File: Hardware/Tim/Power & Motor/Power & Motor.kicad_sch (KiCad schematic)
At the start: 86 parts, among them Q1 BSC520N15NS3, Q2 BSC520N15NS3, Q3 BSC093N15NS5, Q4 BSC093N15NS5, Q5 BSC520N15NS3, Q6 BSC520N15NS3, Q7 BSC093N15NS5, Q8 BSC093N15NS5, U1 LTC7810, U2 LTC7810, U3 LTC6908-2

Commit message: motor controller and h-bridge stuff
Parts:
- added C53, C54, C59: 0.1uF, symbol Device:C_Small
- added C55, C56: 1uF, symbol Device:C_Small
- added C57: 47uF, symbol Device:C_Polarized_Small
- added C58: 150uF, symbol Device:C_Polarized_Small
- added M1: Motor_DC_ALT, symbol Motor:Motor_DC_ALT
- added Q10, Q11, Q12, Q9: Q_NMOS_SGD, symbol Device:Q_NMOS_SGD
- added R10: 10K, symbol Device:R_Small
- added R7: idk, symbol Device:R_Small
- added U4: DRV8714, DRV8714_RHA_TEX, symbol BPP_Lib:DRV8714
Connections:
- net GND: now also C56.2, C57.2, C58.2, C59.2, Q10.1 (S), Q12.1 (S), U4.19 (PGND1), U4.37 (GND), U4.41 (GND)
- net +24V: no longer names the net of C37.2, C38.1, C40.1, C41.1, C42.1, C43.1, C44.1, C45.1, C46.1, C47.1, C48.1, L3.2, L4.2, R14.1, R15.2, R16.1, U2.1 (SENSE1-), U2.11 (EXTVCC), U2.12 (SENSE2-)
- net +24V: no longer C16.1, C17.1, C18.1, C19.1, C2.2, C20.1, C21.1, C22.1, C23.1, C3.1, L1.2, L2.2, R3.1, R4.2, R5.1, U1.1 (SENSE1-), U1.11 (EXTVCC), U1.12 (SENSE2-)
- new net: C53.1, U4.26 (CP1H)
- new net: C53.2, U4.25 (CP1L)
- new net: C54.2, U4.23 (CP2L)
- new net: C54.1, U4.24 (CP2H)
- new net: C55.2, U4.27 (VCP)
- new net BRAKE: U4.11 (BRAKE)
- new net FAULT: R10.2, U4.8 (NFLT)
- new net GH1: Q9.2 (G), U4.16 (GH1)
- new net GH2: Q11.2 (G), U4.22 (GH2)
- new net GL1: Q10.2 (G), U4.18 (GL1)
- new net GL2: Q12.2 (G), U4.20 (GL2)
- new net IN1: U4.3 (IN1/EN1)
- new net IN2: U4.4 (IN2/PH1)
- new net NSLEEP: U4.7 (NSLEEP)
- new net SH1: Q10.3 (D), Q9.1 (S), R7.1, U4.12 (SP1), U4.17 (SH1)
- new net SH2: M1.2 (-), Q11.1 (S), Q12.3 (D), U4.21 (SH2)
- new net SN1: M1.1 (+), R7.2, U4.13 (SN1)
- new net SO1: U4.9 (SO1)
- new net VCC: C16.1, C17.1, C18.1, C19.1, C2.2, C20.1, C21.1, C22.1, C23.1, C3.1, C55.1, C56.1, C57.1, C58.1, C59.1, L1.2, L2.2, Q11.3 (D), Q9.3 (D), R10.1, R3.1, R4.2, R5.1, U1.1 (SENSE1-), U1.11 (EXTVCC), U1.12 (SENSE2-), U4.28 (PVDD), U4.38 (DVDD)
- no-connect marks 2 -> 15
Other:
- note added: "0.1uF x 2"
- note added: "20V Dual Phase, Single Output, Step-Down Regulator"
- note added: "H-Bridge"
- note added: "Motor Controller"
- note added: "Motor Driver"
- note added: "Switching Controller"
- note removed: "20V Four Phase, Single Output, Step-Down Regulator"
- note removed: "Switching Controllers"
- moved on the sheet: BT1, C24, C25, C26, C27, C28, C29, C30, C31, C32, C33, C34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

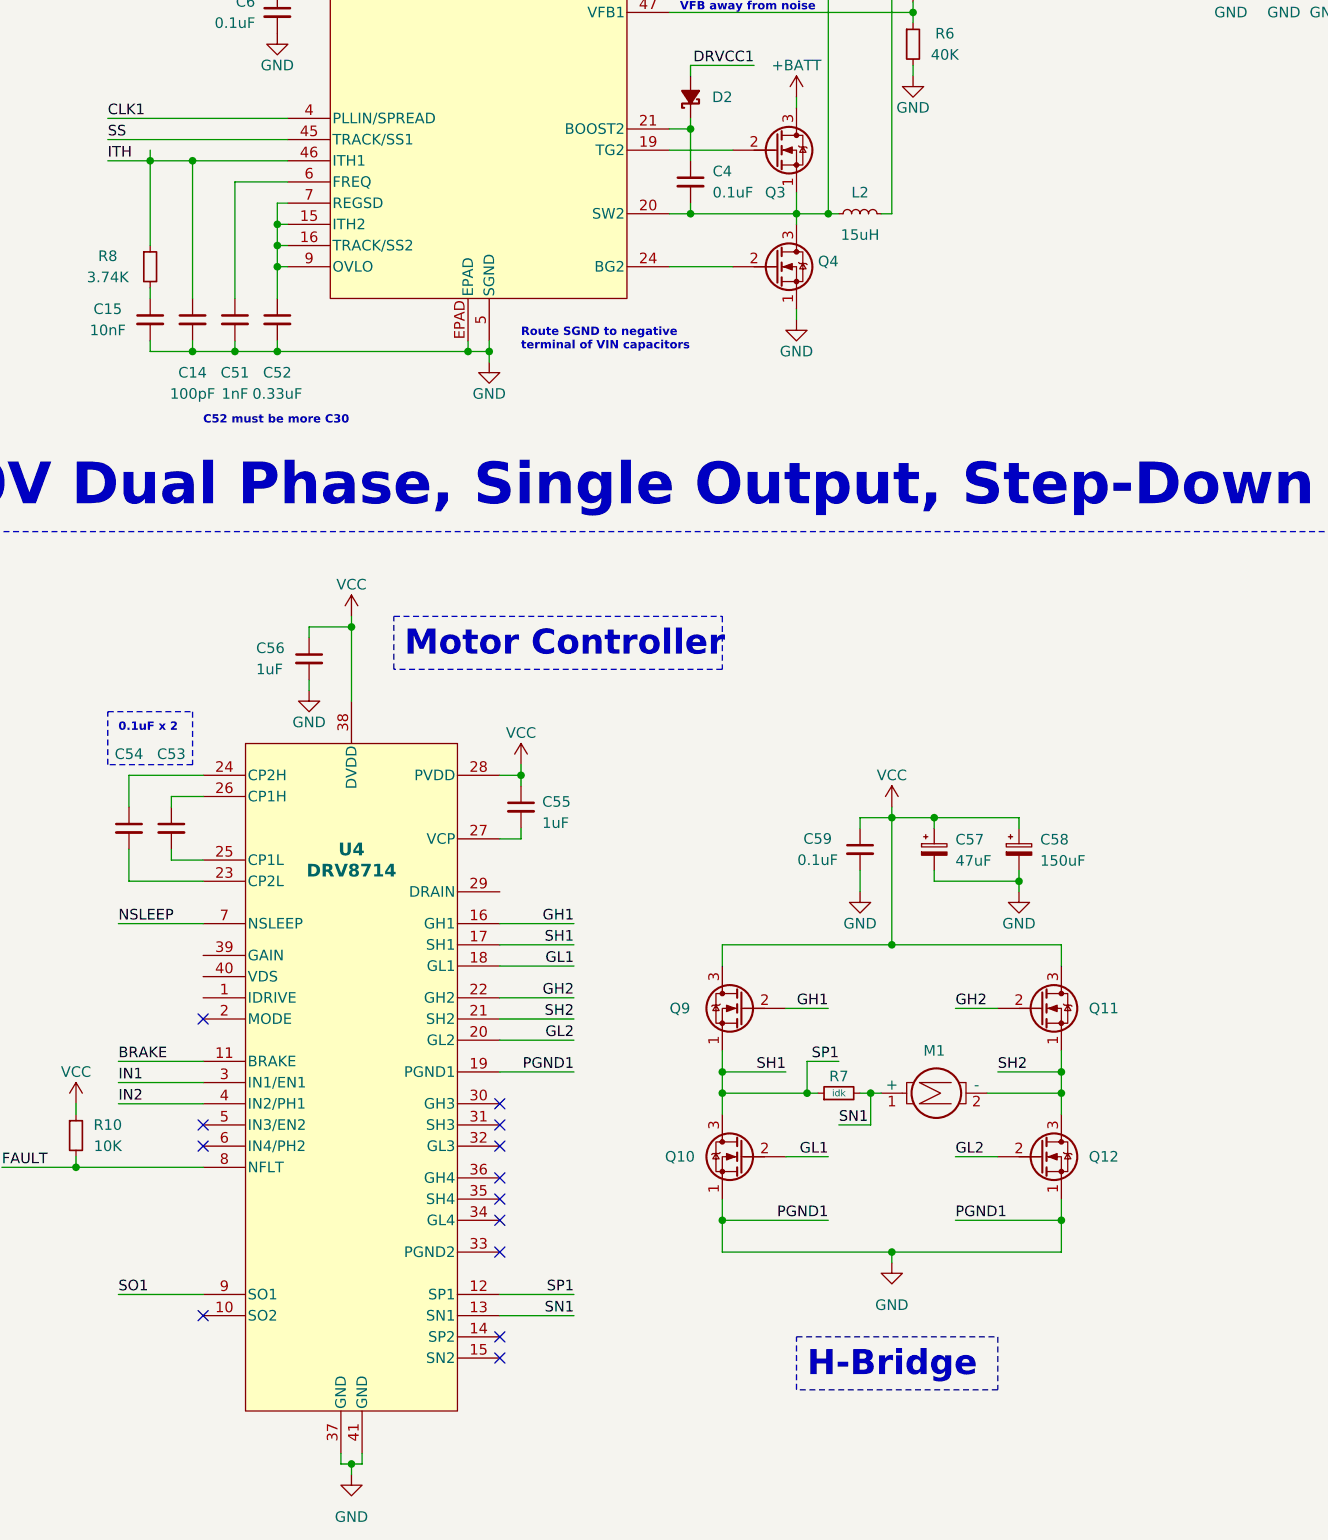
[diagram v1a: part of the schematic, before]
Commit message: more h-bridge shenanigans and 2 phase power (cringe)
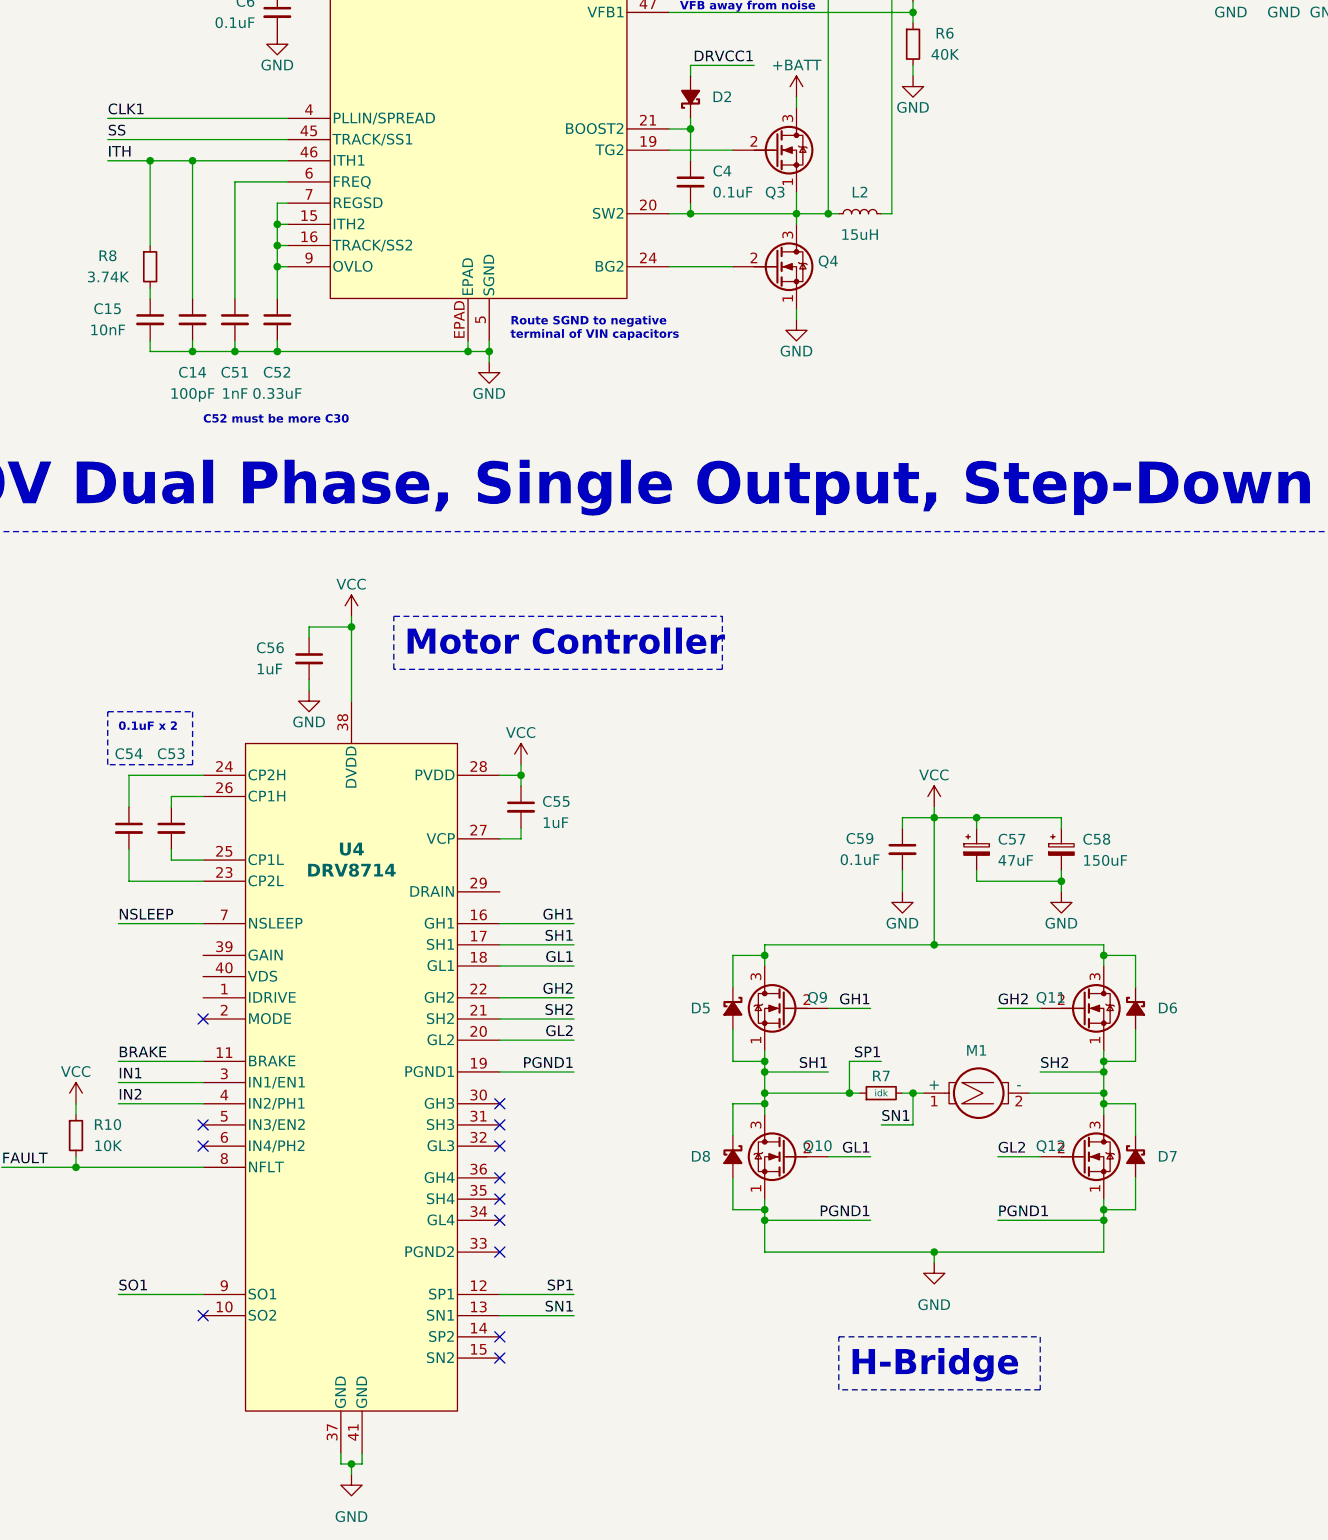
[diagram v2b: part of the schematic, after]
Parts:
- added D5, D6, D7, D8: D_Schottky_Small_Filled, symbol Device:D_Schottky_Small_Filled
- Q10, Q11, Q12, Q9: value Q_NMOS_SGD -> BSC010N04LSATMA1; footprint (none) -> BPP_Lib:Infineon 8-PowerTDFN
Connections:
- net GND: now also D7.2 (A), D8.2 (A)
- net SH1: now also D5.2 (A), D8.1 (K)
- net SH2: now also D6.2 (A), D7.1 (K)
- net VCC: now also D5.1 (K), D6.1 (K)
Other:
- moved on the sheet: C57, C58, C59, M1, Q10, Q11, Q12, Q9, R7

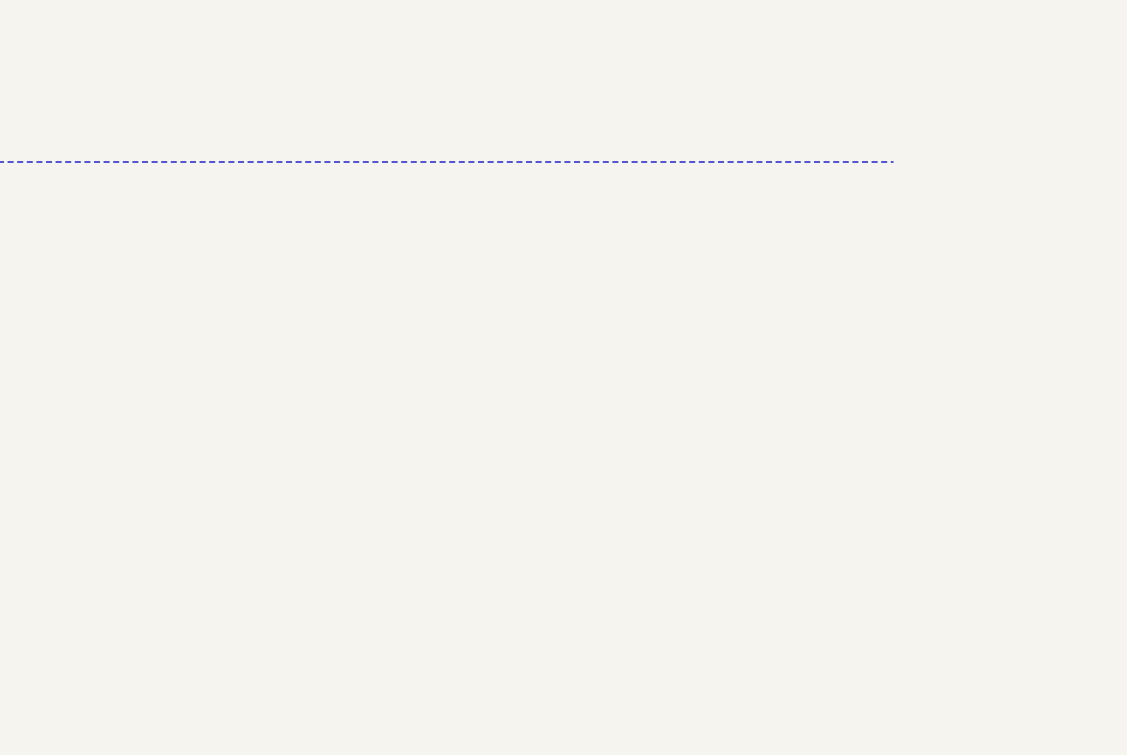
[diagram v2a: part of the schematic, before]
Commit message: Made it all one board due to large space allowed
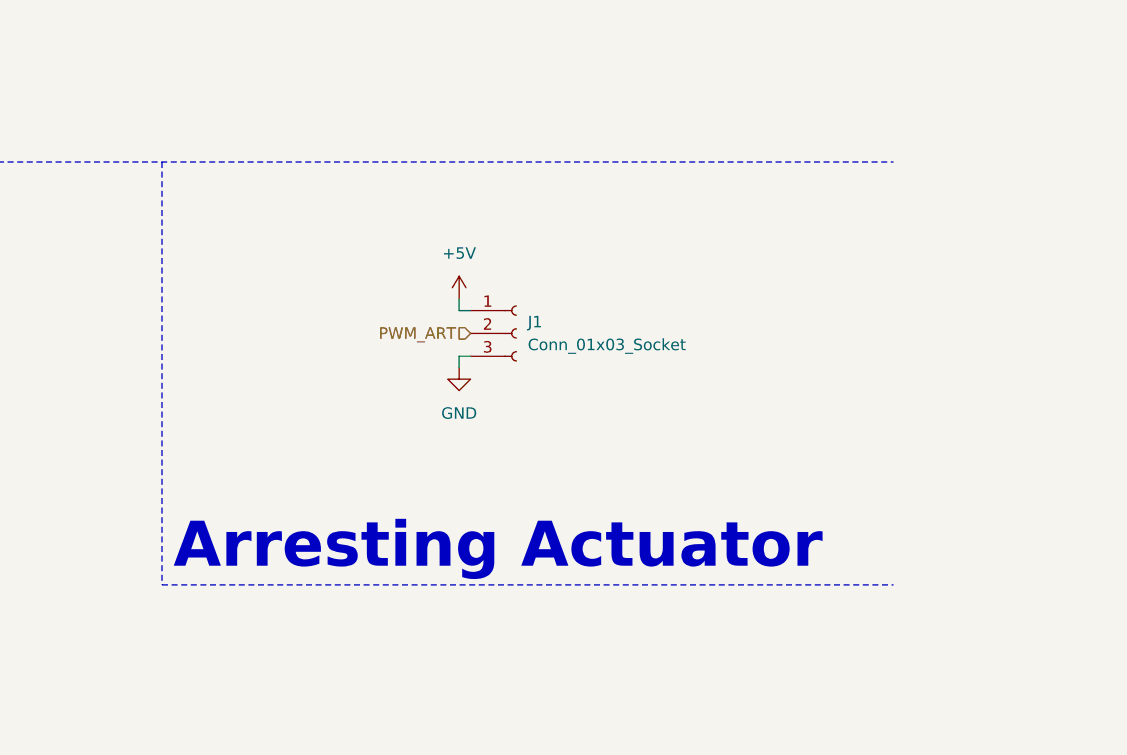
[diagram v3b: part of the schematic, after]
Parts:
- added J1: Conn_01x03_Socket, symbol Connector:Conn_01x03_Socket
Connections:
- net GND: now also J1.3 (Pin_3)
- new net +5V: J1.1 (Pin_1)
- new net PWM_ART: J1.2 (Pin_2)
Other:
- note added: "Arresting Actuator"
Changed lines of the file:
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@@
     (stroke (width 0) (type default))
   )
+  (wire (pts (xy 360.68 171.45) (xy 359.41 171.45))
+    (stroke (width 0) (type default))
+  )
   (wire (pts (xy 497.84 -19.05) (xy 492.76 -19.05))
     (stroke (width 0) (type default))
@@
     (stroke (width 0) (type default))
   )
+  (wire (pts (xy 359.41 166.37) (xy 360.68 166.37))
+    (stroke (width 0) (type default))
+  )
   (wire (pts (xy 110.49 69.85) (xy 110.49 71.12))
     (stroke (width 0) (type default))
@@
     (stroke (width 0) (type default))
   )
+  (wire (pts (xy 359.41 171.45) (xy 359.41 172.72))
+    (stroke (width 0) (type default))
+  )
   (wire (pts (xy 114.3 217.17) (xy 124.46 217.17))
     (stroke (width 0) (type default))
@@
     (stroke (width 0) (type default))
   )
+  (wire (pts (xy 359.41 165.1) (xy 359.41 166.37))
+    (stroke (width 0) (type default))
+  )
   (wire (pts (xy 55.88 78.74) (xy 55.88 83.82))
     (stroke (width 0) (type default))
@@
     (stroke (width 0) (type default))
   )
+  (polyline (pts (xy 326.39 149.86) (xy 326.39 196.85))
+    (stroke (width 0) (type dash_dot))
+  )
   (wire (pts (xy 55.88 76.2) (xy 55.88 78.74))
     (stroke (width 0) (type default))
@@
     (stroke (width 0) (type default))
   )
+  (polyline (pts (xy 326.39 196.85) (xy 407.67 196.85))
+    (stroke (width 0) (type dash_dot))
+  )
   (wire (pts (xy 375.92 36.83) (xy 381 36.83))
     (stroke (width 0) (type default))
@@
     (effects (font (size 3 3) (thickness 0.6) bold) (justify left bottom))
   )
+  (text "Arresting Actuator" (at 327.66 195.58 0)
+    (effects (font (size 5 5) (thickness 1) bold) (justify left bottom))
+  )
   (text "330uF x 2" (at 175.26 68.58 0)
     (effects (font (size 1 1) (thickness 0.2) bold) (justify left bottom))
@@
     (effects (font (size 1.27 1.27)) (justify right bottom))
   )
+  (hierarchical_label "PWM_ART" (shape input) (at 360.68 168.91 180) (fields_autoplaced)
+    (effects (font (size 1.27 1.27)) (justify right))
+  )
   (symbol (lib_id "power:VCC") (at 85.09 177.8 0) (unit 1)
     (in_bom yes) (on_board yes) (dnp no) (fields_autoplaced)
@@
     )
   )
+  (symbol (lib_id "Connector:Conn_01x03_Socket") (at 365.76 168.91 0) (unit 1)
+    (in_bom yes) (on_board yes) (dnp no) (fields_autoplaced)
+    (property "Reference" "J1" (at 367.03 167.64 0)
+      (effects (font (size 1.27 1.27)) (justify left))
+    )
+    (property "Value" "Conn_01x03_Socket" (at 367.03 170.18 0)
+      (effects (font (size 1.27 1.27)) (justify left))
+    )
+    (property "Footprint" "" (at 365.76 168.91 0)
+      (effects (font (size 1.27 1.27)) hide)
+    )
+    (property "Datasheet" "~" (at 365.76 168.91 0)
+      (effects (font (size 1.27 1.27)) hide)
+    )
+    (pin "1")
+    (pin "2")
+    (pin "3")
+    (instances
+      (project "Power & Motor"
+        (path "/83758ee8-f9c9-4fb9-a75c-cd41edea6d26"
+          (reference "J1") (unit 1)
+        )
+      )
+    )
+  )
   (symbol (lib_id "power:GND") (at 149.86 193.04 0) (unit 1)
     (in_bom yes) (on_board yes) (dnp no)
@@
     )
   )
+  (symbol (lib_id "power:+5V") (at 359.41 165.1 0) (unit 1)
+    (in_bom yes) (on_board yes) (dnp no) (fields_autoplaced)
+    (property "Reference" "#PWR044" (at 359.41 168.91 0)
+      (effects (font (size 1.27 1.27)) hide)
+    )
+    (property "Value" "+5V" (at 359.41 160.02 0)
+      (effects (font (size 1.27 1.27)))
+    )
+    (property "Footprint" "" (at 359.41 165.1 0)
+      (effects (font (size 1.27 1.27)) hide)
+    )
+    (property "Datasheet" "" (at 359.41 165.1 0)
+      (effects (font (size 1.27 1.27)) hide)
+    )
+    (pin "1")
+    (instances
+      (project "Power & Motor"
+        (path "/83758ee8-f9c9-4fb9-a75c-cd41edea6d26"
+          (reference "#PWR044") (unit 1)
+        )
+      )
+    )
+  )
   (symbol (lib_id "Device:C_Small") (at 55.88 87.63 0) (unit 1)
     (in_bom yes) (on_board yes) (dnp no)
@@
         )
       )
+    )
+  )
+  (symbol (lib_id "power:GND") (at 359.41 172.72 0) (unit 1)
+    (in_bom yes) (on_board yes) (dnp no) (fields_autoplaced)
+    (property "Reference" "#PWR043" (at 359.41 179.07 0)
+      (effects (font (size 1.27 1.27)) hide)
+    )
+    (property "Value" "GND" (at 359.41 177.8 0)
+      (effects (font (size 1.27 1.27)))
+    )
+    (property "Footprint" "" (at 359.41 172.72 0)
+      (effects (font (size 1.27 1.27)) hide)
+    )
+    (property "Datasheet" "" (at 359.41 172.72 0)
+      (effects (font (size 1.27 1.27)) hide)
+    )
+    (pin "1")
+    (instances
+      (project "Power & Motor"
+        (path "/83758ee8-f9c9-4fb9-a75c-cd41edea6d26"
+          (reference "#PWR043") (unit 1)
+        )
+      )
